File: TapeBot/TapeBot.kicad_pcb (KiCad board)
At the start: 2 copper layers, 152.4 x 101.6 mm, 63 parts, among them J1 43045-0412, J10 9652068, J2 43045-0412, J3 9652068, J4 9652068, J5 9652068, J6 9652068, J7 9652068, J8 9652068, J9 9652068, Q1 MMBT4403, Q2 MMBT4403, U1 HX711HX711, U2 HX711HX711, U3 Teensy4.1, U4 TB6612FNG, U5 TB6612FNG, U6 TB6612FNG, U7 TB6612FNG

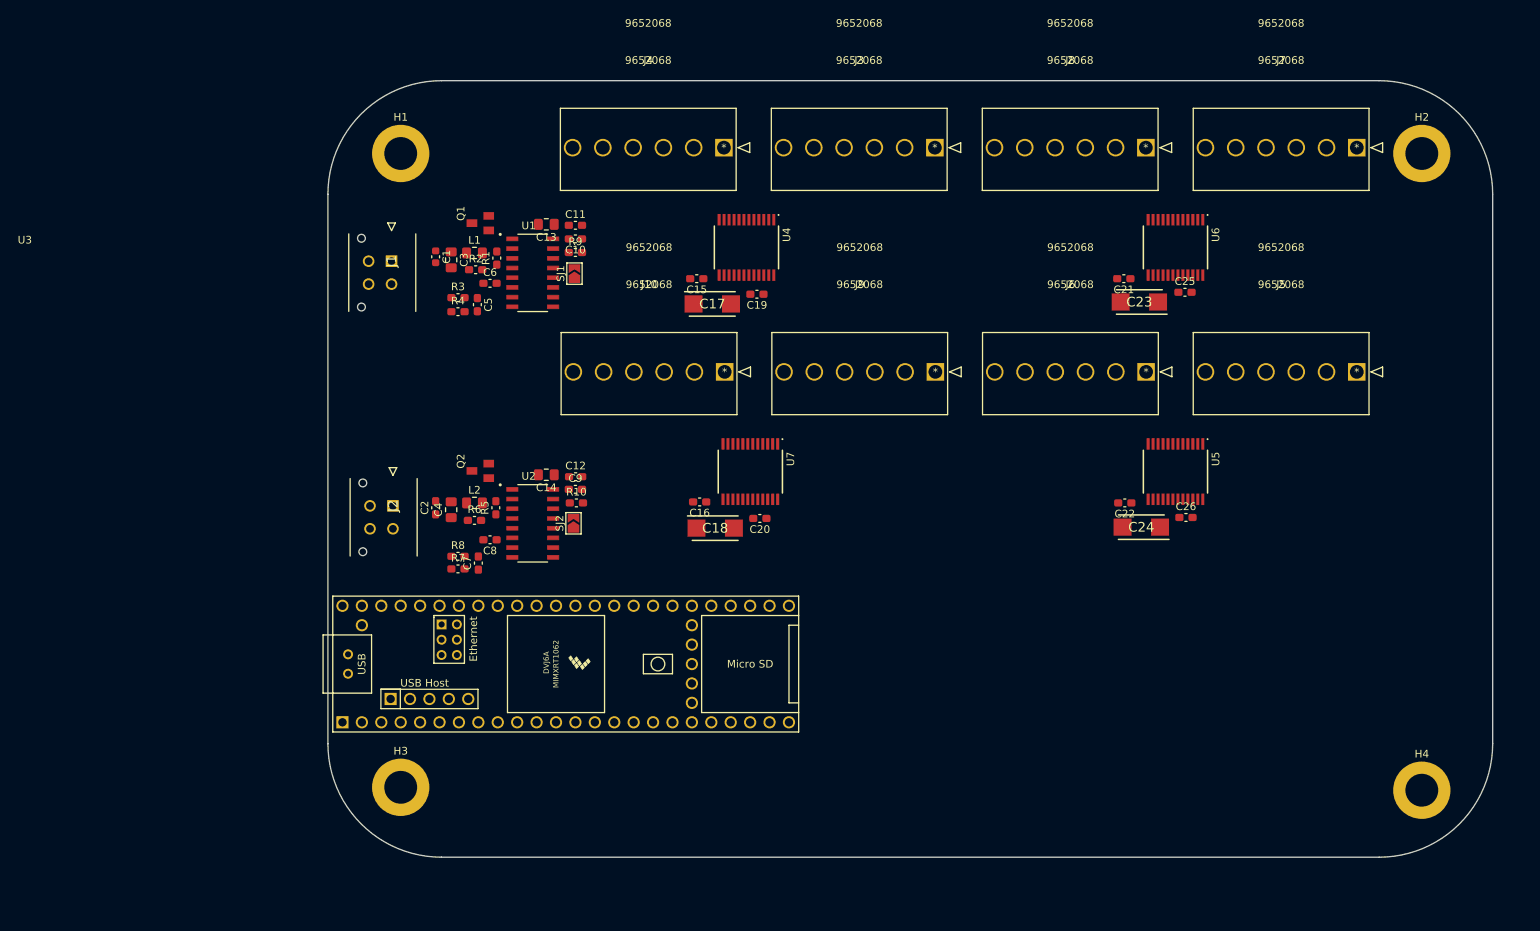
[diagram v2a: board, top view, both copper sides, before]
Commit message: First layout of PCB finished
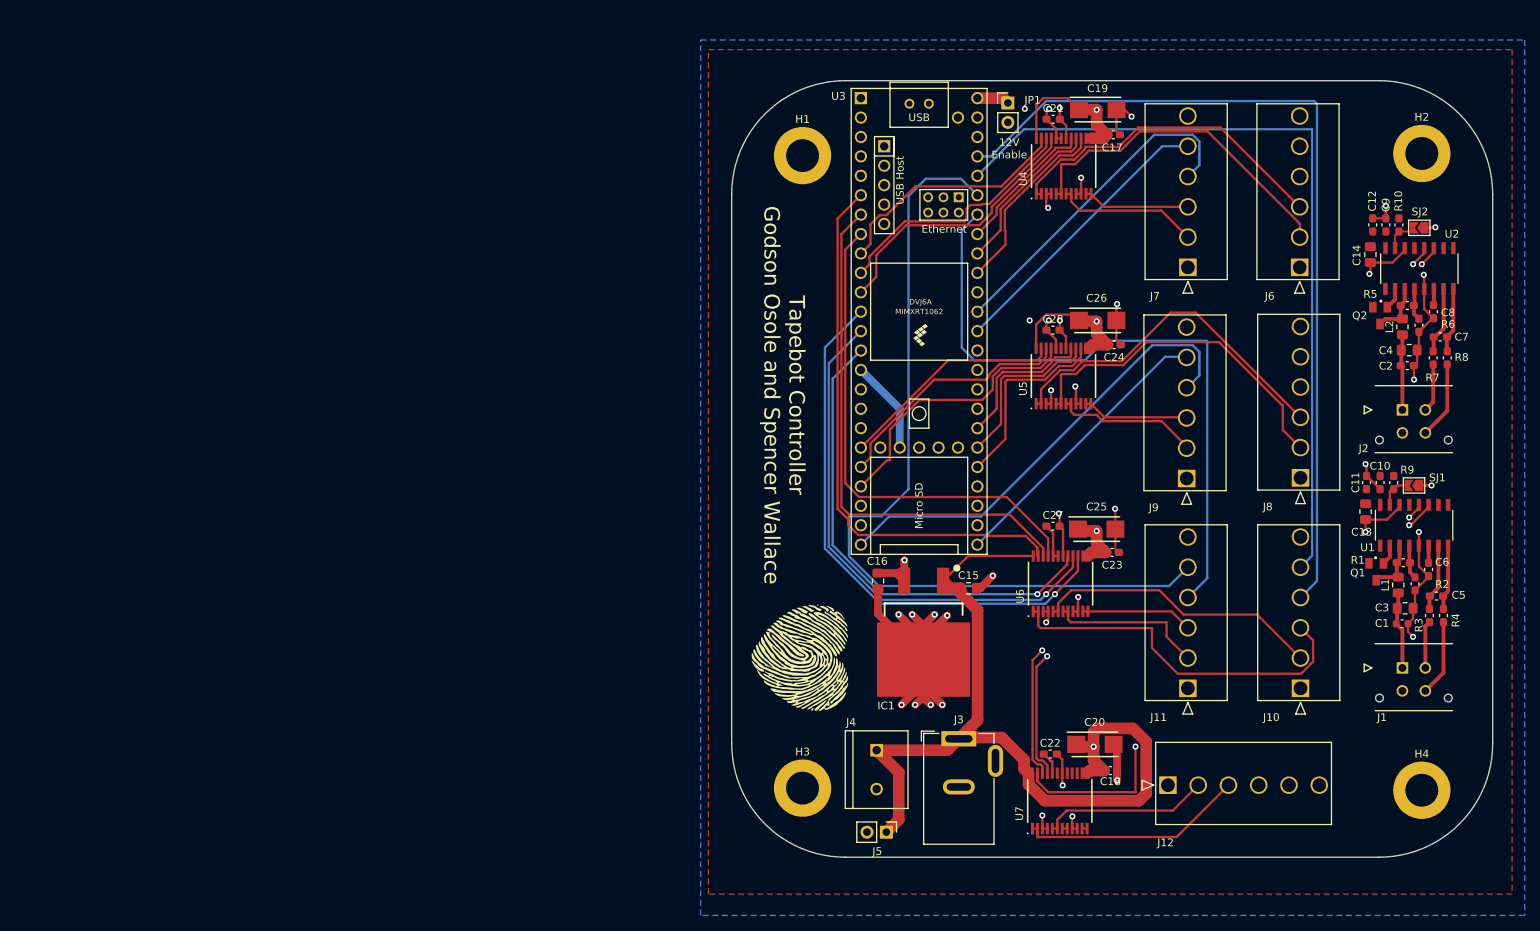
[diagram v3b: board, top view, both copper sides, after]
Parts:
- removed the J10 at (136.0, 71.9)
- added C15: 0.33µF, Capacitor_SMD:C_0805_2012Metric_Pad1.18x1.45mm_HandSolder, F.Cu at (167.9, 100.2)
- added C16: 0.1µF, Capacitor_SMD:C_0805_2012Metric_Pad1.18x1.45mm_HandSolder, F.Cu at (156.0, 99.2)
- added G***: LOGO, tapebot:SmallLogo, F.Cu at (145.8, 109.3)
- added IC1: L7805ABD2T-TR, tapebot:D2PAK-STB35NF10T4, F.Cu at (156.9, 102.2)
- added J3: Barrel_Jack, Connector_BarrelJack:BarrelJack_GCT_DCJ200-10-A_Horizontal, F.Cu at (166.6, 119.9)
- added J4: Conn_01x02, tapebot:TE_282837-2, F.Cu at (155.9, 123.9)
- added J5: Conn_01x02, Connector_PinHeader_2.54mm:PinHeader_1x02_P2.54mm_Vertical, F.Cu at (157.1, 132.1)
- added JP1: Jumper_2_Open, Connector_PinHeader_2.54mm:PinHeader_1x02_P2.54mm_Vertical, F.Cu at (173.0, 36.7)
- J10: renamed from J7; value 9652068 -> CON_9652068_MOL
- J11: renamed from J8; value 9652068 -> CON_9652068_MOL
- J12: renamed from J9; value 9652068 -> CON_9652068_MOL
- J6: renamed from J3; value 9652068 -> CON_9652068_MOL
- J7: renamed from J4; value 9652068 -> CON_9652068_MOL
- J8: renamed from J5; value 9652068 -> CON_9652068_MOL
- J9: renamed from J6; value 9652068 -> CON_9652068_MOL
- moved J1 142.6 mm to (224.7, 110.6), turned to 180 degrees
- moved C1 135.3 mm to (224.6, 104.8), turned to 0 degrees
- moved R4 134.9 mm to (230.0, 103.8), turned to 90 degrees
- moved R3 133.7 mm to (228.2, 103.8), turned to 90 degrees
- moved C3 132.9 mm to (225.0, 102.8), turned to 0 degrees
- moved J2 132.7 mm to (224.7, 76.9), turned to 180 degrees
- moved R8 132.0 mm to (230.5, 70.1), turned to 90 degrees
- moved C5 131.2 mm to (229.1, 101.2), turned to 0 degrees
- moved R7 130.6 mm to (228.7, 70.1), turned to 90 degrees
- moved R2 129.6 mm to (226.3, 99.6), turned to 90 degrees
- moved C7 129.3 mm to (229.6, 67.3), turned to 0 degrees
- moved C2 128.5 mm to (225.3, 71.1), turned to 0 degrees
- moved L1 128.4 mm to (224.1, 99.8), turned to 90 degrees
- moved C6 128.4 mm to (228.1, 97.7), turned to 90 degrees
- moved C4 127.1 mm to (225.6, 69.0), turned to 0 degrees
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- renumbered C15 to C17, C16 to C18, C17 to C19, C18 to C20, C19 to C21, C20 to C22, C21 to C23, C22 to C24, C23 to C25, C24 to C26, C25 to C27, C26 to C28
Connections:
- U3 pad 13: M4_CTL1 -> M4_CTL2
- U3 pad 14: M4_CTL2 -> M4_CTL1
- U3 pad 19: M5_CTL2 -> M5_PWM
- U3 pad 2: M8_CTL1 -> unconnected-(U3-Pad2)
- U3 pad 20: M5_CTL1 -> M5_CTL2
- U3 pad 21: M5_PWM -> M5_CTL1
- U3 pad 26: M7_CTL2 -> M7_PWM
- U3 pad 27: M7_CTL1 -> M7_CTL2
- U3 pad 28: M7_PWM -> M7_CTL1
- U3 pad 30: M6_CTL1 -> M6_CTL2
- U3 pad 31: M6_CTL2 -> M6_CTL1
- U3 pad 35: M8_PWM -> unconnected-(U3-Pad35)
- U3 pad 39: M2_CTL2 -> M2_PWM
- U3 pad 40: M2_CTL1 -> M2_CTL2
- U3 pad 41: M2_PWM -> M2_CTL1
- U3 pad 48: unconnected-(U3-Pad48) -> Net-(JP1-Pad1)
- U3 pad 6: M3_CTL2 -> M3_PWM
- U3 pad 7: M3_CTL1 -> M3_CTL2
- U3 pad 8: M3_PWM -> M3_CTL1
- U7 pad 11: /MotorDrivers/8B01 -> unconnected-(U7-Pad11)
- U7 pad 12: /MotorDrivers/8B01 -> unconnected-(U7-Pad11)
- U7 pad 15: M8_PWM -> /MotorDrivers/8PWMB
- U7 pad 16: M8_CTL2 -> /MotorDrivers/8BIN2
- U7 pad 17: M8_CTL1 -> /MotorDrivers/8BIN1
- U7 pad 7: /MotorDrivers/8B02 -> unconnected-(U7-Pad7)
- U7 pad 8: /MotorDrivers/8B02 -> unconnected-(U7-Pad7)
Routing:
- net +12V: track 0.00 -> 247.0 mm, vias 0 -> 4
- net GND: track 0.00 -> 185.0 mm, vias 0 -> 35
- net M3_OUT2: track 0.00 -> 113.1 mm
- net M4_OUT1: track 0.00 -> 110.7 mm
- net M3_OUT1: track 0.00 -> 104.3 mm
- net +3.3V: track 0.00 -> 88.0 mm, vias 0 -> 4
- net M4_OUT2: track 0.00 -> 86.7 mm
- net L2_SCK: track 0.00 -> 82.9 mm, vias 0 -> 1
- net M7_OUT1: track 0.00 -> 77.7 mm
- net +5V: track 0.00 -> 76.7 mm, vias 0 -> 1
- net M5_OUT2: track 0.00 -> 73.6 mm
- net M4_PWM: track 0.00 -> 72.8 mm, vias 0 -> 1
- net M3_PWM: track 0.00 -> 72.1 mm
- net L1_SCK: track 0.00 -> 71.1 mm, vias 0 -> 1
- net M3_CTL2: track 0.00 -> 69.0 mm
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- added copper zone on F.Cu, net +3.3V
- added copper zone on B.Cu, net GND
- added copper zone on In1.Cu, net GND
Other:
- board size 152.4 x 101.6 mm -> 99.6 x 101.6 mm
- copper layers 2 -> 4
- board text added: "12V Enable"
- board text added: "Tapebot Controller Godson Osole and Spencer Wallace"
- board text added: "Wallace"

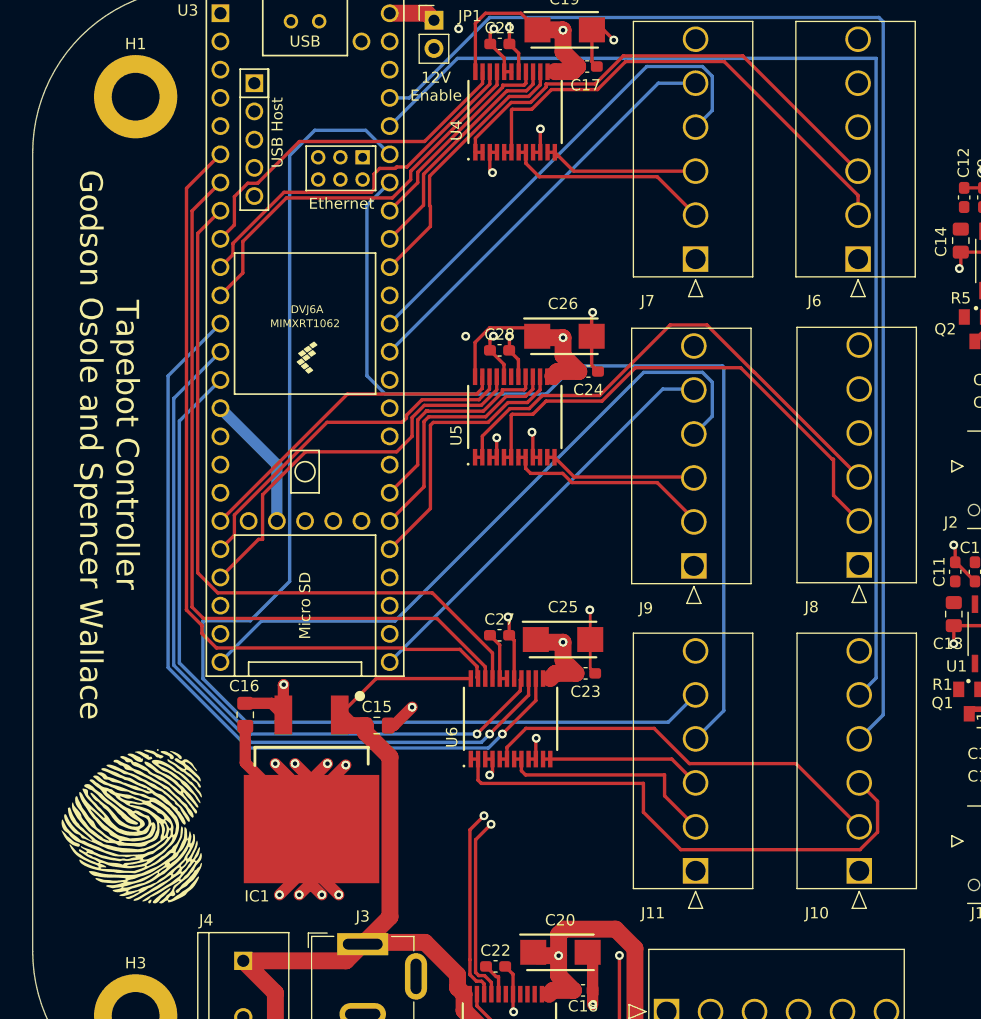
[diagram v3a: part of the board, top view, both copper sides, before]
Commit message: Fixed Voltage Regulator placement, Added ground vias
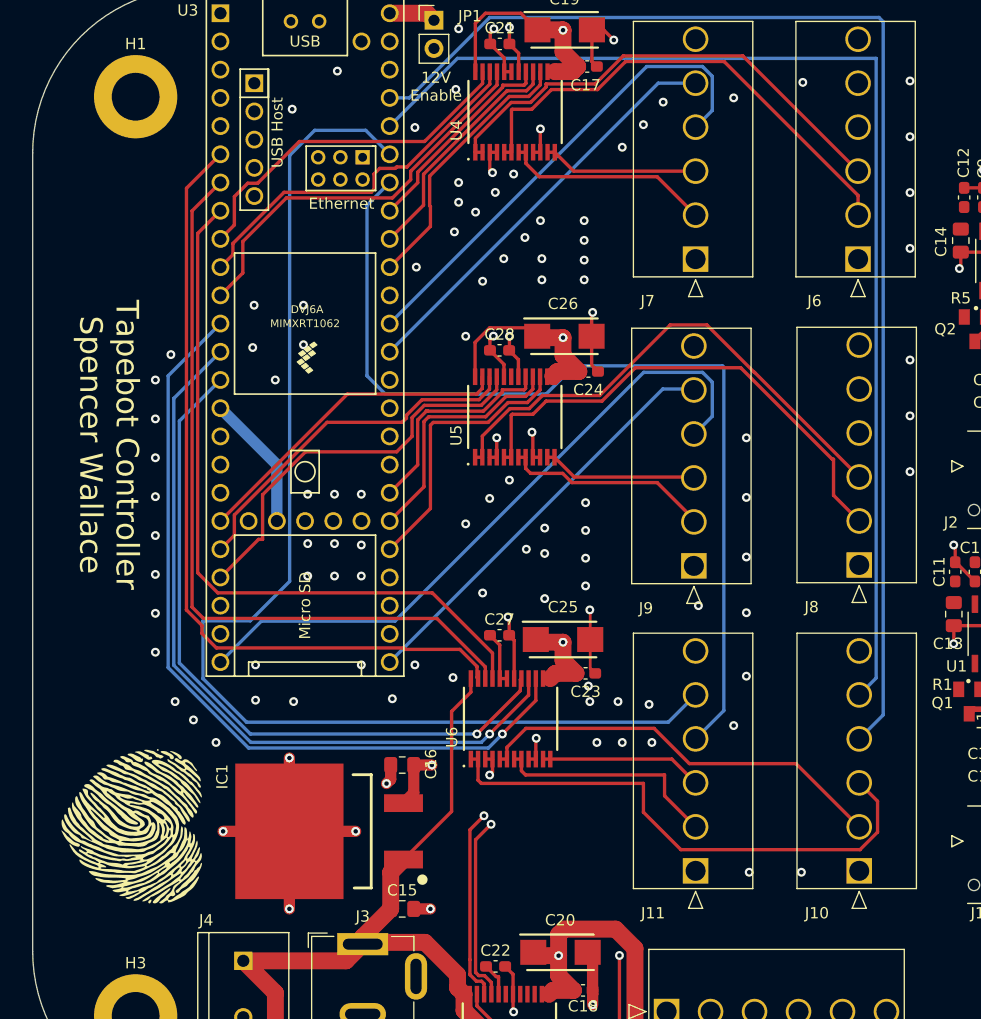
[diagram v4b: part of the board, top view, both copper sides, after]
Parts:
- moved C15 16.7 mm to (170.2, 116.7)
- moved C16 14.8 mm to (170.2, 103.8), turned to 180 degrees
- moved IC1 10.8 mm to (167.4, 104.6), turned to 0 degrees
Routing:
- net GND: track 185.0 -> 145.3 mm, vias 35 -> 126
- net +12V: track 247.0 -> 237.5 mm
- net +5V: track 76.7 -> 70.0 mm
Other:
- board text added: "Tapebot Controller Spencer Wallace"
- board text removed: "Tapebot Controller Godson Osole and Spencer Wallace"
